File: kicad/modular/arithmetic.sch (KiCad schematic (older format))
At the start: 29 parts

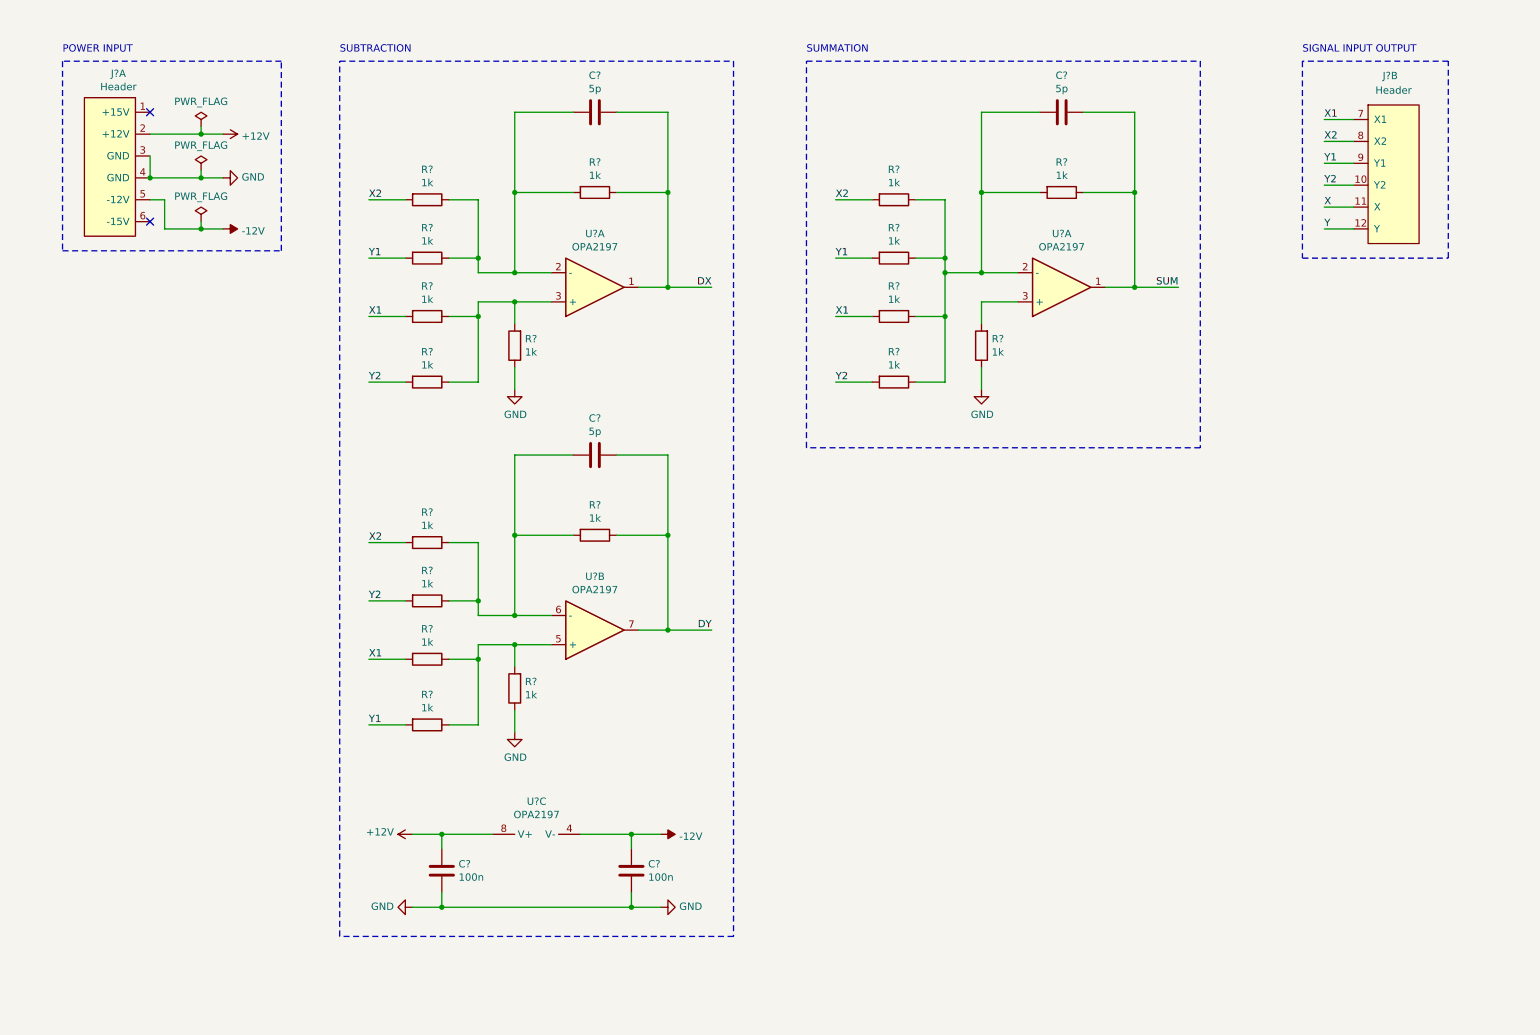
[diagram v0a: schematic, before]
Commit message: completed schematic of arthimetic board
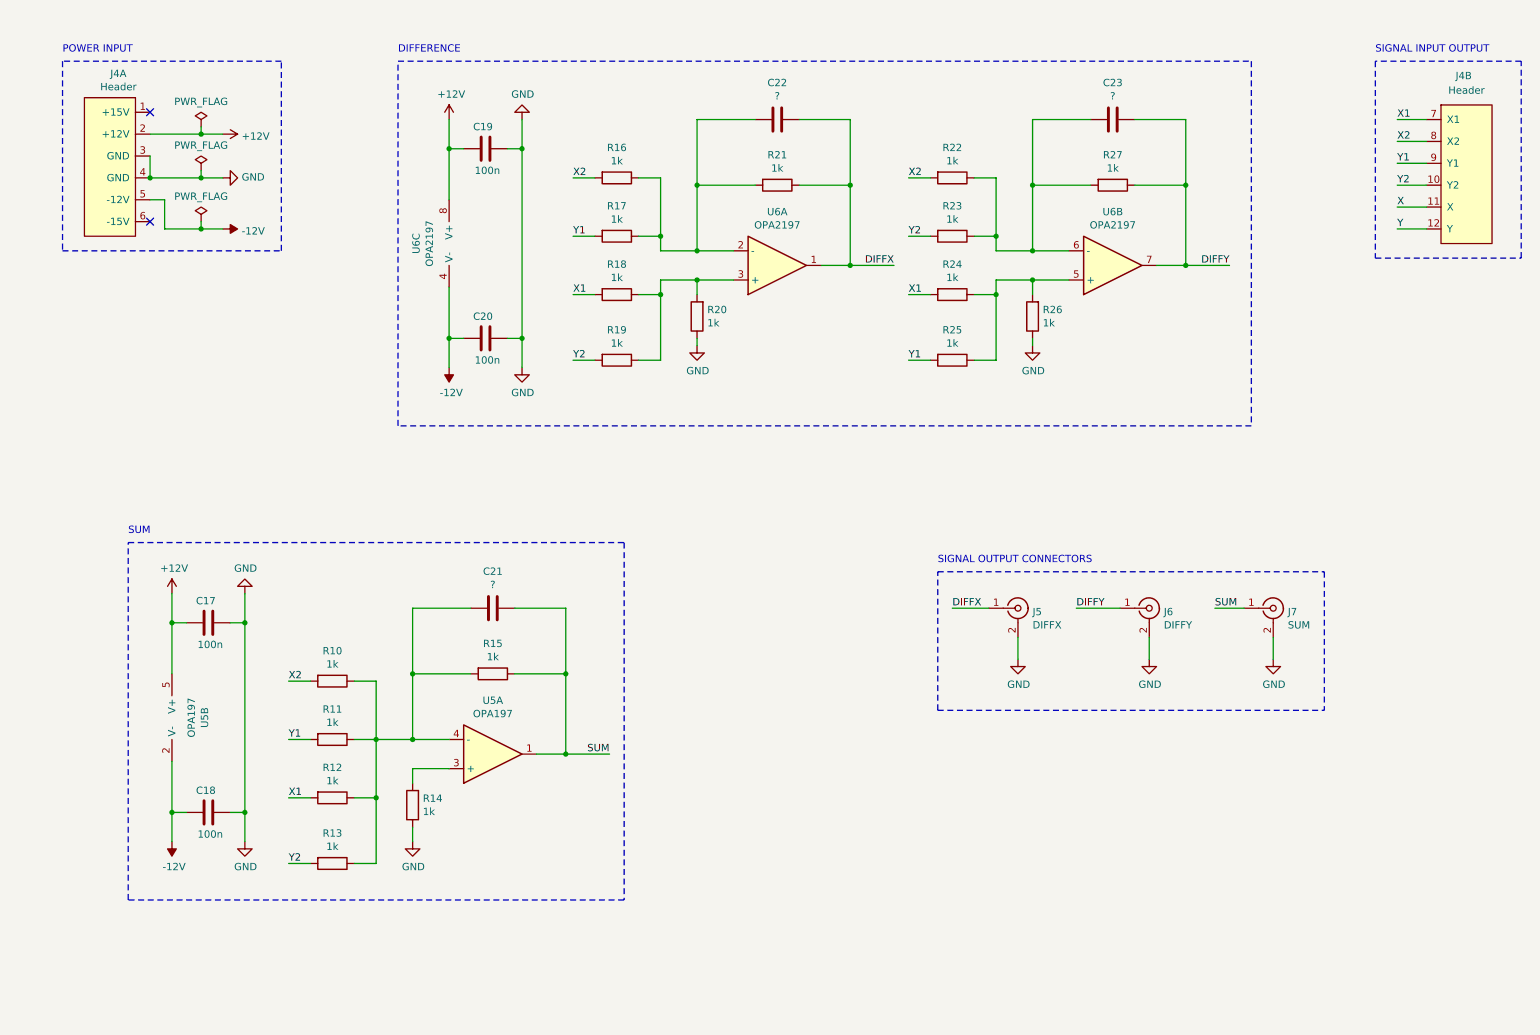
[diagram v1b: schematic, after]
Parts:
- removed U?: OPA2197, symbol Device:Opamp_Dual_Generic
- added C17, C18: 100n, Capacitor_SMD:C_0603_1608Metric, symbol Device:C
- added J5: DIFFX, Connector_Coaxial:SMA_Amphenol_901-144_Vertical, symbol Connector:Conn_Coaxial
- added J6: DIFFY, Connector_Coaxial:SMA_Amphenol_901-144_Vertical, symbol Connector:Conn_Coaxial
- added J7: SUM, Connector_Coaxial:SMA_Amphenol_901-144_Vertical, symbol Connector:Conn_Coaxial
- added U5: OPA197, Connector_Coaxial:SMA_Amphenol_901-144_Vertical, symbol Device:Opamp_Generic
- C19, C20: renamed from C?; footprint (none) -> Capacitor_SMD:C_0603_1608Metric
- C21, C22, C23: renamed from C?; value 5p -> ?; footprint (none) -> Capacitor_SMD:C_0603_1608Metric
- J4: renamed from J?; footprint (none) -> Connector_Header:PinHeader_2.54mm
- R10, R11, R12, R13, R14, R15, R16, R17, R18, R19, R20, R21, R22, R23, R24, R25, R26, R27: renamed from R?; footprint (none) -> Resistor_SMD:R_0603_1608Metric
- U6: renamed from U?; footprint (none) -> Connector_Coaxial:SMA_Amphenol_901-144_Vertical
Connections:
- net +12V: now also C17.1, U5.5 (V+)
- net -12V: now also C18.1, U5.2 (V-)
- net GND: now also C17.2, C18.2, J5.2 (Ext), J6.2 (Ext), J7.2 (Ext)
- net SUM: now also J7.1 (In), U5.1
- net at C21.2, R10.1, R11.1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: now also U5.4 (-)
- net at R14.2: now also U5.3 (+)
- net DX renamed DIFFX
- net DIFFX: now also J5.1 (In)
- net DY renamed DIFFY
- net DIFFY: now also J6.1 (In)
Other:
- note added: "DIFFERENCE"
- note added: "SIGNAL OUTPUT CONNECTORS"
- note added: "SUM"
- note removed: "SUBTRACTION"
- note removed: "SUMMATION"
- moved on the sheet: C19, C20, C21, C22, C23, J4B, R10, R11, R12, R13, R14, R15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

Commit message: added pcb design of arithmetic board
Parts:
- removed U6: OPA2197, Connector_Coaxial:SMA_Amphenol_901-144_Vertical, symbol Device:Opamp_Dual_Generic
- added C24, C25: 100n, Capacitor_SMD:C_0603_1608Metric, symbol Device:C
- added U7, U8: OPA197, OPA197IDR:SOIC127P600X175-8N, symbol Device:Opamp_Generic
- U5: footprint Connector_Coaxial:SMA_Amphenol_901-144_Vertical -> OPA197IDR:SOIC127P600X175-8N
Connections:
- net +12V: now also C24.1, U7.5 (V+), U8.5 (V+)
- net -12V: now also C25.1, U7.2 (V-), U8.2 (V-)
- net DIFFX: now also U7.1
- net DIFFY: now also U8.1
- net GND: now also C24.2, C25.2
- net at C22.2, R16.1, R17.1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: now also U7.4 (-)
- net at R18.1, R19.1, R20.2: now also U7.3 (+)
- net at C23.2, R22.1, R23.1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: now also U8.4 (-)
- net at R24.1, R25.1, R26.2: now also U8.3 (+)
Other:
- note added: "DIFFX"
- note added: "DIFFY"
- note removed: "DIFFERENCE"
- moved on the sheet: C17, C18, C19, C20, C21, C22, C23, J4A, J5, J6, J7, R10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

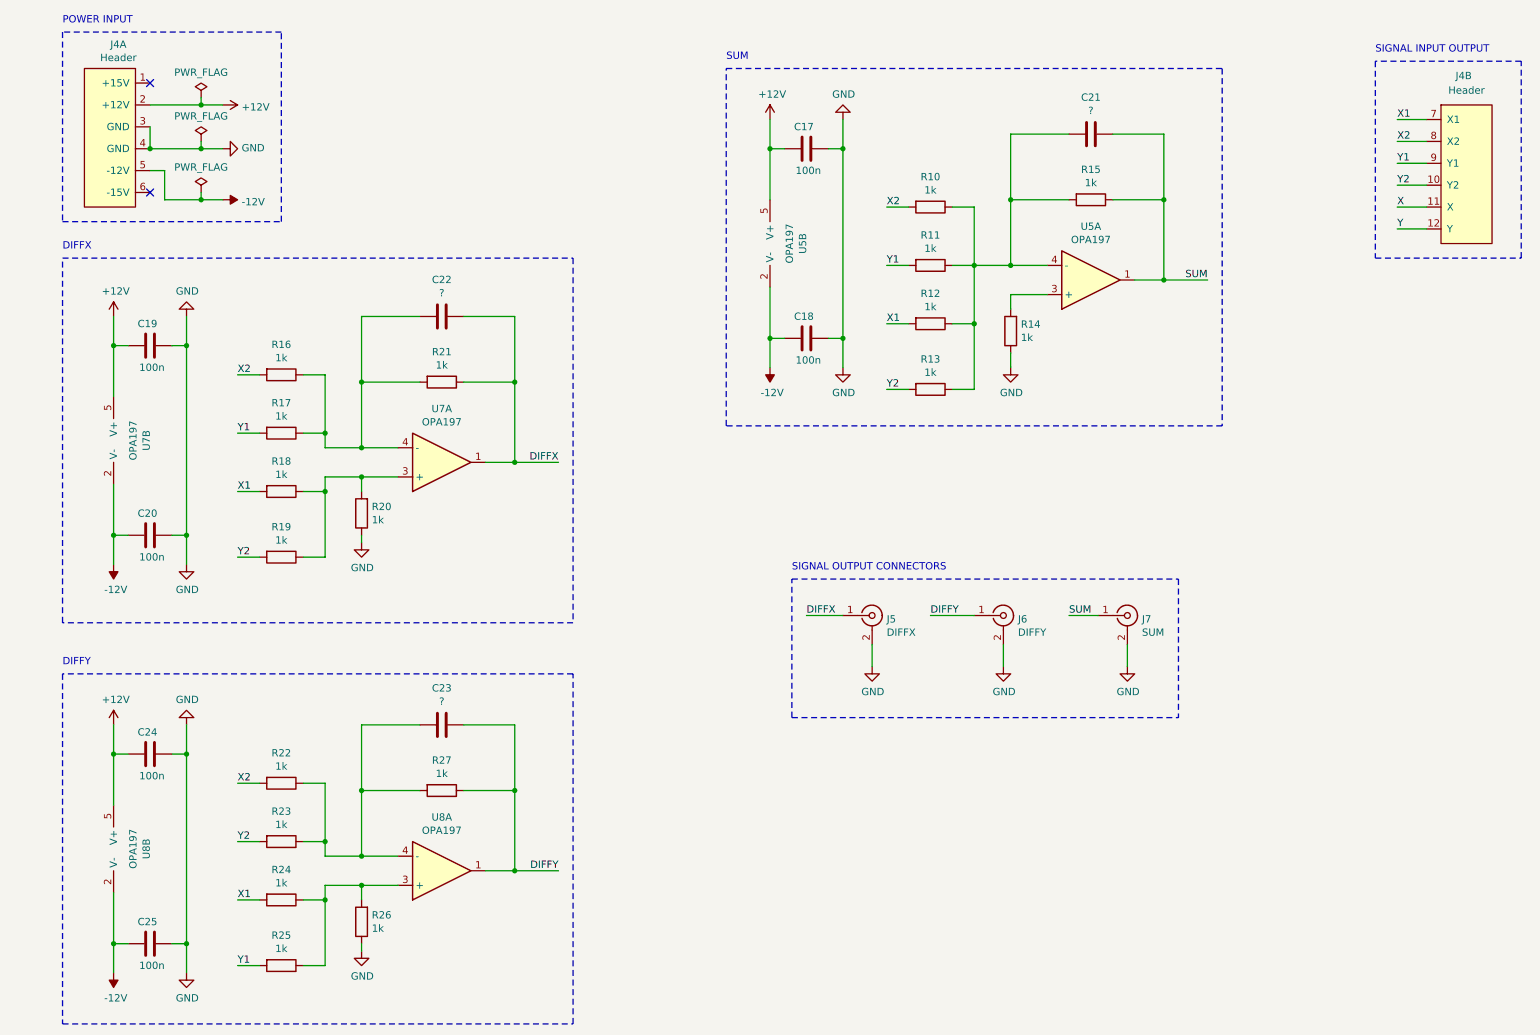
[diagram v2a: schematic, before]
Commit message: updated arithmetic schematic with resistor arrays and dual opamp, removed old footprints
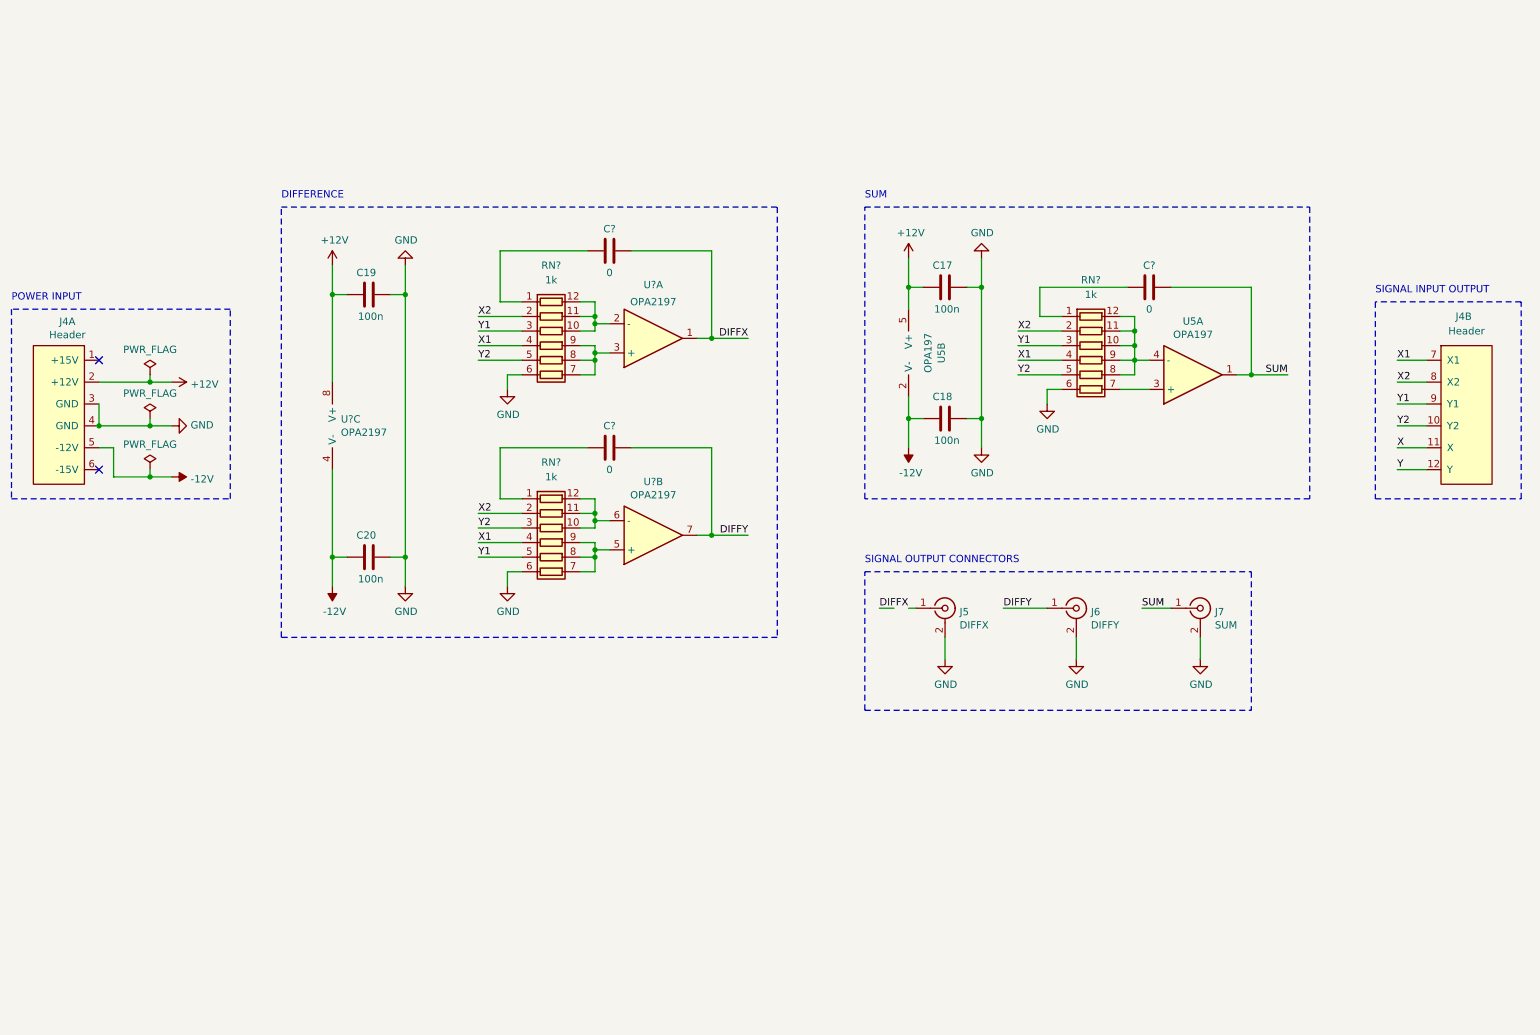
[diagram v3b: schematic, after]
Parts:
- removed C21, C22, C23: ?, Capacitor_SMD:C_0603_1608Metric, symbol Device:C
- removed C24, C25: 100n, Capacitor_SMD:C_0603_1608Metric, symbol Device:C
- removed R10, R11, R12, R13, R14, R15, R16, R17, R18, R19, R20, R21, R22, R23, R24, R25, R26, R27: 1k, Resistor_SMD:R_0603_1608Metric, symbol Device:R
- removed U7, U8: OPA197, OPA197IDR:SOIC127P600X175-8N, symbol Device:Opamp_Generic
- added C? (x3): 0, symbol Device:C
- added RN? (x3): 1k, symbol Device:R_Pack06
- added U? (x3): OPA2197, symbol Device:Opamp_Dual_Generic
- J5, J6, J7: footprint Connector_Coaxial:SMA_Amphenol_901-144_Vertical -> Connector_SMA:SMA_Molex_73251-2120_EdgeMount
- U5: footprint OPA197IDR:SOIC127P600X175-8N -> Package_SO:SOIC-8_3.9x4.9mm_P1.27mm
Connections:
- net +12V: now also U?.8 (V+)
- net -12V: now also U?.4 (V-)
- net DIFFX: now also C?.1, U?.1; no longer J5.1 (In)
- net DIFFY: now also C?.1, U?.7
- net GND: now also RN?.6 (R6.1), RN?.6 (R6.1), RN?.6 (R6.1)
- net SUM: now also C?.1
- net X1: now also RN?.4 (R4.1), RN?.4 (R4.1), RN?.4 (R4.1)
- net X2: now also RN?.2 (R2.1), RN?.2 (R2.1), RN?.2 (R2.1)
- net Y1: now also RN?.3 (R3.1), RN?.3 (R3.1), RN?.5 (R5.1)
- net Y2: now also RN?.3 (R3.1), RN?.5 (R5.1), RN?.5 (R5.1)
- net at U5.3 (+): now also RN?.7 (R6.2)
- net at U5.4 (-): now also RN?.10 (R3.2), RN?.11 (R2.2), RN?.12 (R1.2), RN?.8 (R5.2), RN?.9 (R4.2)
- new net: C?.2, RN?.1 (R1.1) (x3)
- new net: RN?.10 (R3.2), RN?.11 (R2.2), RN?.12 (R1.2), U?.2 (-)
- new net: RN?.7 (R6.2), RN?.8 (R5.2), RN?.9 (R4.2), U?.3 (+)
- new net: RN?.10 (R3.2), RN?.11 (R2.2), RN?.12 (R1.2), U?.6 (-)
- new net: RN?.7 (R6.2), RN?.8 (R5.2), RN?.9 (R4.2), U?.5 (+)
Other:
- note added: "DIFFERENCE"
- note removed: "DIFFX"
- note removed: "DIFFY"
- moved on the sheet: C17, C18, C19, C20, J4A, J4B, J5, J6, J7, U5A, U5B

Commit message: applied pcb design feedback to arithmetic board
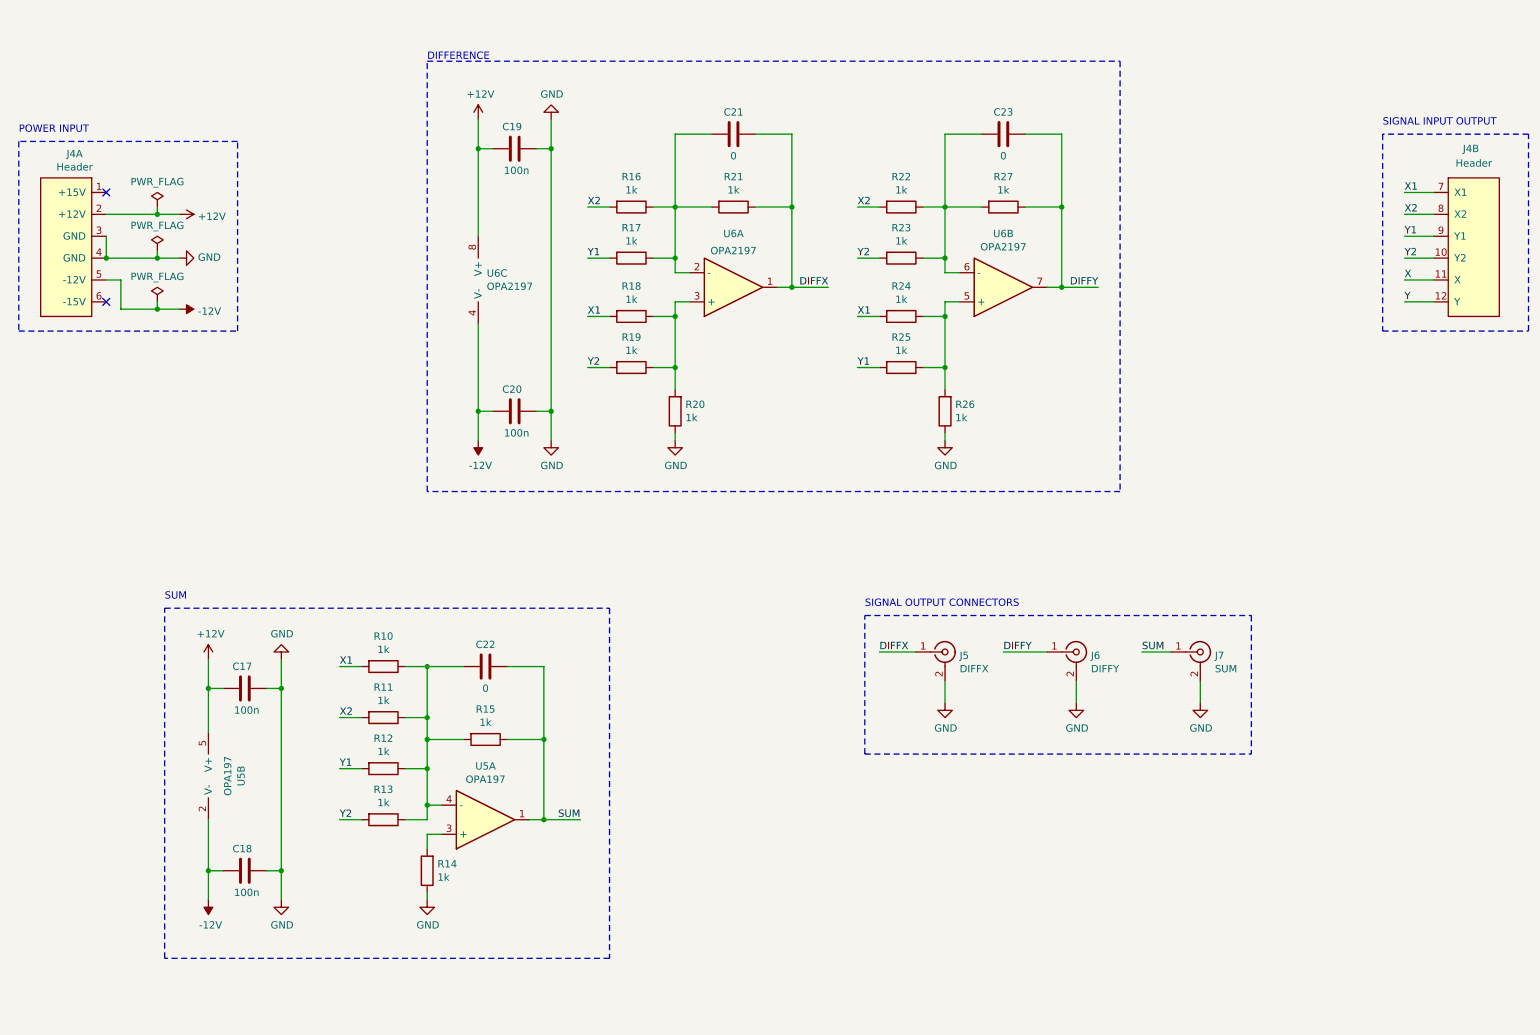
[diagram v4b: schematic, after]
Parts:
- removed C? (x2): 0, symbol Device:C
- removed RN? (x3): 1k, symbol Device:R_Pack06
- added C22, C23: 0, Capacitor_SMD:C_0603_1608Metric, symbol Device:C
- added R10, R11, R12, R13, R14, R15, R16, R17, R18, R19, R20, R21, R22, R23, R24, R25, R26, R27: 1k, Resistor_SMD:R_0603_1608Metric, symbol Device:R
- C21: renamed from C?; footprint (none) -> Capacitor_SMD:C_0603_1608Metric
- U6: renamed from U?; footprint (none) -> Package_SO:SOIC-8_3.9x4.9mm_P1.27mm
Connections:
- net DIFFX: now also J5.1 (In), R21.1
- net DIFFY: now also C23.1, R27.1
- net GND: now also R14.1, R20.1, R26.1
- net SUM: now also C22.1, R15.1
- net X1: now also R10.2, R18.2, R24.2
- net X2: now also R11.2, R16.2, R22.2
- net Y1: now also R12.2, R17.2, R25.2
- net Y2: now also R13.2, R19.2, R23.2
- net at U5.3 (+): now also R14.2
- net at U5.4 (-): now also C22.2, R10.1, R11.1, R12.1, R13.1, R15.2
- net at C21.2: now also U6.2 (-), R16.1, R17.1, R21.2
- net at U6.3 (+): now also R18.1, R19.1, R20.2
- net at U6.6 (-): now also C23.2, R22.1, R23.1, R27.2
- net at U6.5 (+): now also R24.1, R25.1, R26.2
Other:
- moved on the sheet: C17, C18, C19, C20, C21, J4A, J4B, J5, J6, J7, U5A, U5B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
